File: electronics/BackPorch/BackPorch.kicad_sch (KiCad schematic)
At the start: 15 parts, among them J1 RJ45, J2 RJ45, J3 2601-1102, J4 2601-1104, J5 2601-1104, J6 2601-1104

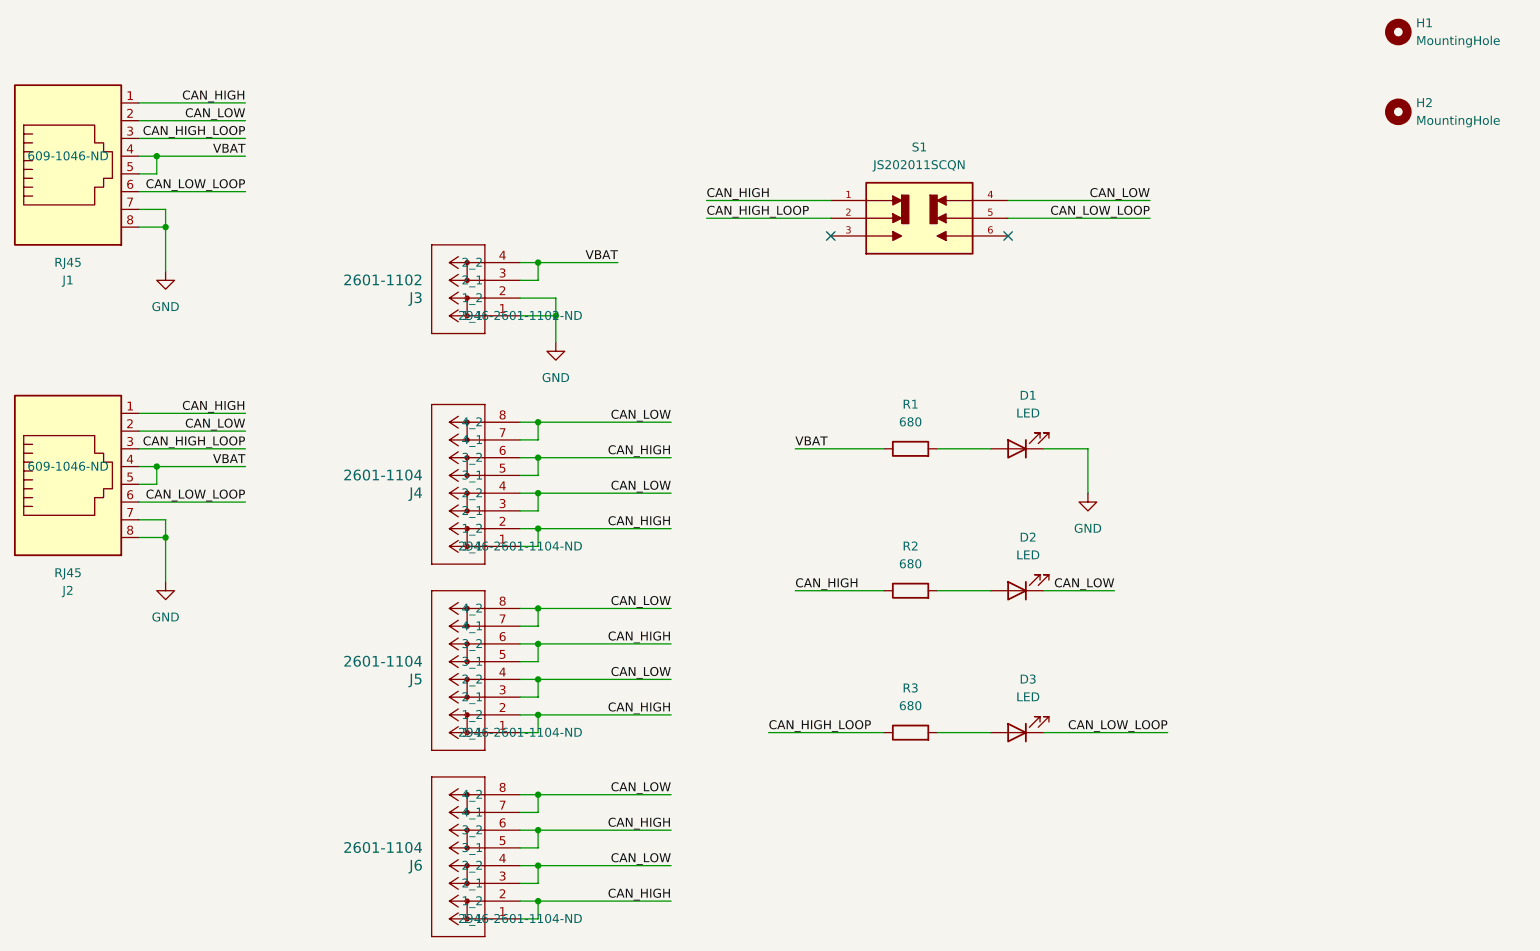
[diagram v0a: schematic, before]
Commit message: Pulling Rev B into main (#1)
* Planning on ordering more back porches.
* Various updates to the footprints. Added datasheets.
* Added the software.
* Verified CAN, voltage input, current reading although the resistor is off, and temperature reading.
* Many updates to get things dialed in. Have the ABS signal working. But there is a small glitch to it.
* Inc encoder is now working as well.
* Added a bootloader.

* Bootloader is working to the point it can push new images into app code space.

* Refactored the CAN messages. Programming is working, at least pushing code. Build version strings are working correctly.

* Refactored the CAN messages. Programming is working, at least pushing code. Build version strings are working correctly.

* Bootblock will reboot on watchdog and stay in the bootblock.

* Forgot to add the auto increment version.

* Updated the bootblock functionality. I am able to program an app code image now.

* I can now reprogram app code from app code.

* Bootloading is working well.

* Updated the README file. It still needs some work.

* The bootblock now allows me to reprogram the bootblock.

* Many refactors to support different deviceIDs. Currently app code can't write to FLASH.

* This is mostly working.

* Things are working well. I can reprogram different units. The CAN status LED flashes as heartbeat messages come in.

* In the app added CAN bus utilization, sorted by device ID. Changed to the release build for the backporch, changed task names, moved can TX tasks into one thread and CAN Rx tasks into a second thread. Fixed a bug with the bootloader picking up the wrong device ID.

* Added the wpilib code. I have only tested the Java code and it works.
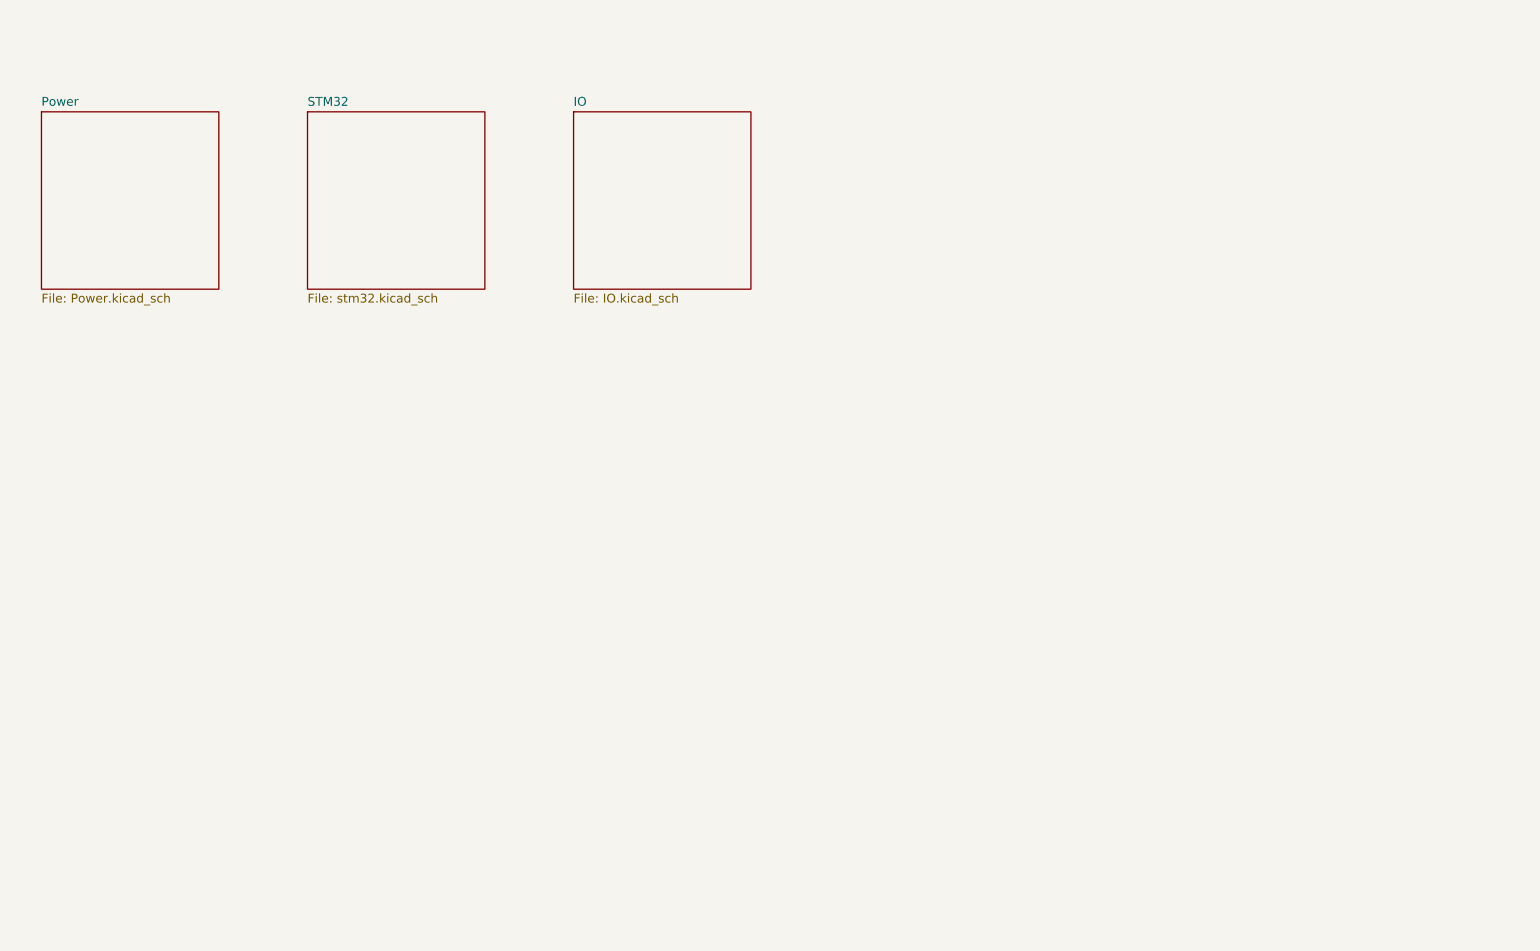
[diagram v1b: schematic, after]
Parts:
- removed D1, D2, D3: LED, LED_SMD:LED_0603_1608Metric, symbol Device:LED
- removed H1, H2: MountingHole, MountingHole:MountingHole_3.2mm_M3, symbol Mechanical:MountingHole
- removed J1, J2: RJ45, LocalFootprints:AMPHENOL_54602-908LF, symbol Connector:RJ45
- removed J3: 2601-1102, LocalFootprints:CONN2_2601-1102_WAG, symbol LocalSyms:WAGO 2601-1102
- removed J4, J5, J6: 2601-1104, LocalFootprints:CONN4_2601-1104_WAG, symbol LocalSyms:WAGO 2601-1104
- removed R1, R2, R3: 680, Resistor_SMD:R_0603_1608Metric, symbol Device:R
- removed S1: JS202011SCQN, LocalFootprints:SW_JS202011SCQN, symbol LocalSyms:JS202011SCQN
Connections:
- no-connect marks 2 -> 0
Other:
- added sheet IO (IO.kicad_sch)
- added sheet Power (Power.kicad_sch)
- added sheet STM32 (stm32.kicad_sch)
